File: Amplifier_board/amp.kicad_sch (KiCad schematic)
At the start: 42 parts, among them J11 Conn_01x03_Pin, J15 Conn_01x03_Pin, U4 TPA3111D1PWPR

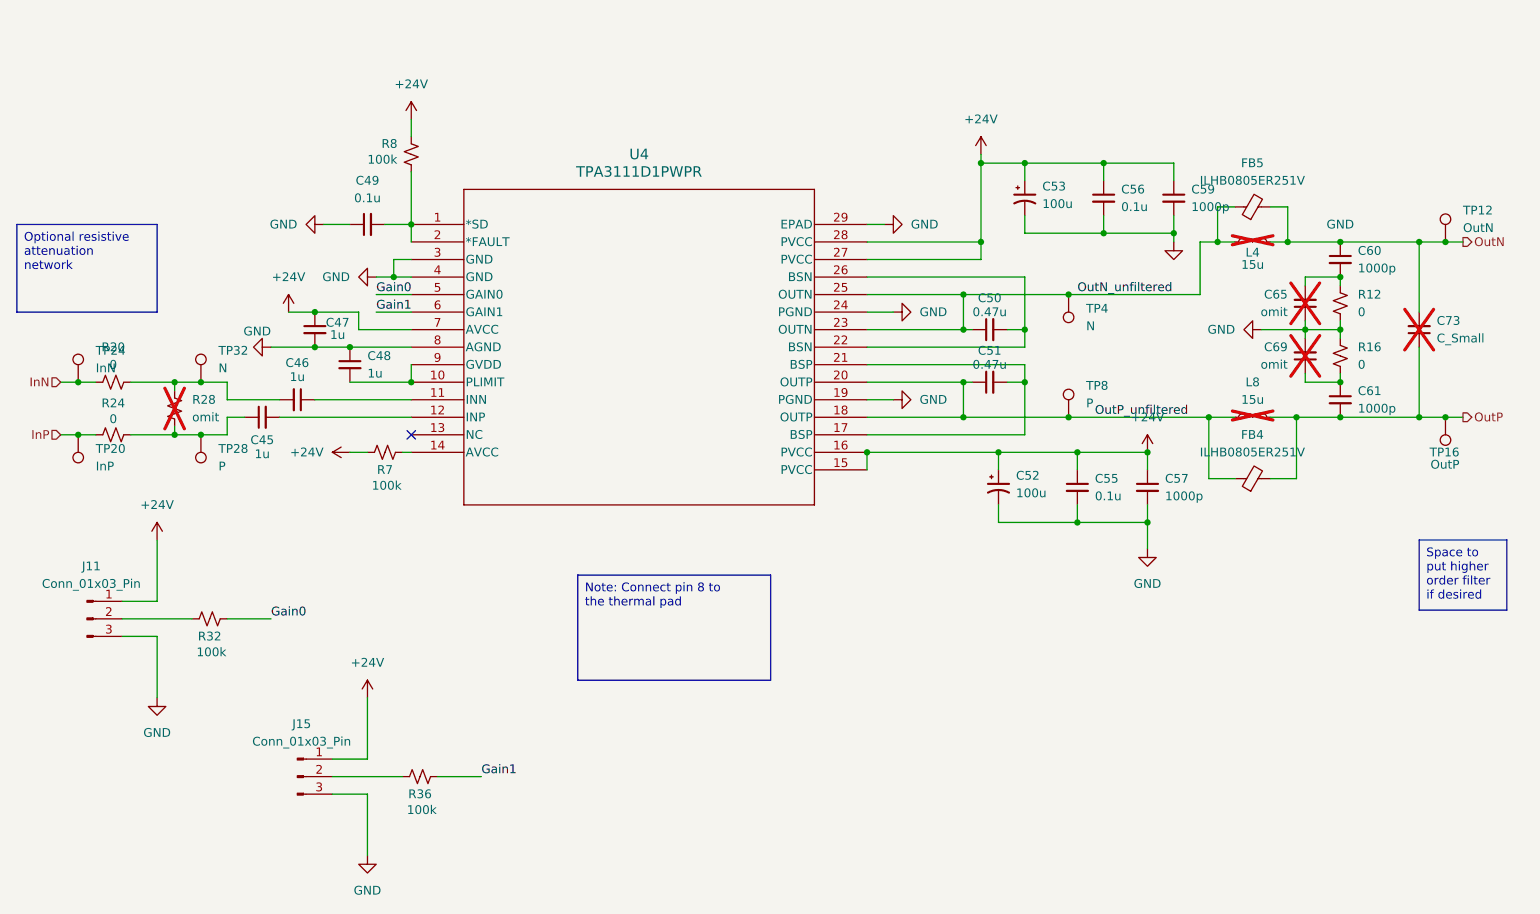
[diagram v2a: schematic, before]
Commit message: Separated AVDD and PVDD on amplifier board
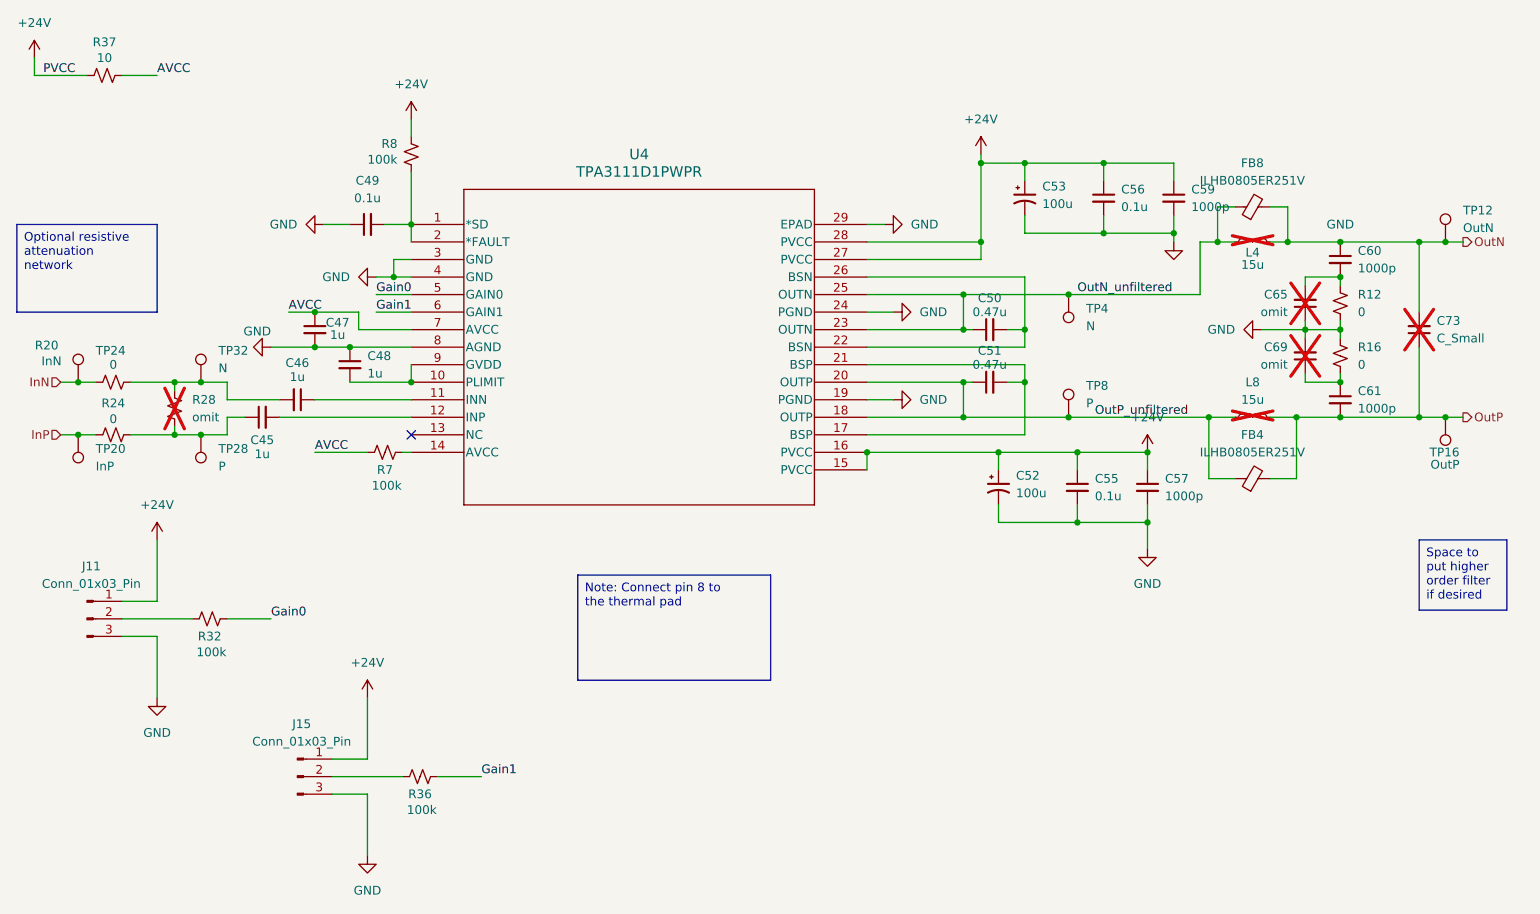
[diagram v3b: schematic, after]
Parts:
- added R37: 10, Capacitor_SMD:C_0805_2012Metric_Pad1.18x1.45mm_HandSolder, symbol Device:R_Small_US
- renumbered FB5 to FB8
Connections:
- net +24V: now also R37.1; no longer C47.1, R7.1, U4.7 (AVCC)
- new net AVCC: C47.1, R37.2, R7.1, U4.7 (AVCC)
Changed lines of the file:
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@@
 	(wire
 		(pts
-			(xy 213.36 62.23) (xy 213.36 64.77)
+			(xy 60.96 41.91) (xy 66.04 41.91)
 		)
 		(stroke
@@
 	(wire
 		(pts
-			(xy 72.39 93.98) (xy 76.2 93.98)
+			(xy 213.36 62.23) (xy 213.36 64.77)
 		)
 		(stroke
@@
 	(wire
 		(pts
-			(xy 93.98 96.52) (xy 96.52 96.52)
+			(xy 72.39 93.98) (xy 76.2 93.98)
 		)
 		(stroke
@@
 	(wire
 		(pts
+			(xy 48.26 39.37) (xy 48.26 41.91)
+		)
+		(stroke
+			(width 0)
+			(type default)
+		)
+	)
+	(wire
+		(pts
 			(xy 102.87 91.44) (xy 83.82 91.44)
 		)
@@
 	(wire
 		(pts
+			(xy 88.9 96.52) (xy 96.52 96.52)
+		)
+		(stroke
+			(width 0)
+			(type default)
+		)
+	)
+	(wire
+		(pts
 			(xy 209.55 106.68) (xy 209.55 104.14)
 		)
@@
 	(wire
 		(pts
+			(xy 48.26 41.91) (xy 55.88 41.91)
+		)
+		(stroke
+			(width 0)
+			(type default)
+		)
+	)
+	(wire
+		(pts
 			(xy 182.88 86.36) (xy 184.15 86.36)
 		)
@@
 		)
 	)
+	(label "AVCC"
+		(at 88.9 96.52 0)
+		(fields_autoplaced yes)
+		(effects
+			(font
+				(size 1.27 1.27)
+			)
+			(justify left bottom)
+		)
+	)
 	(label "OutN_unfiltered"
 		(at 199.39 73.66 0)
@@
 		)
 	)
+	(label "PVCC"
+		(at 49.53 41.91 0)
+		(fields_autoplaced yes)
+		(effects
+			(font
+				(size 1.27 1.27)
+			)
+			(justify left bottom)
+		)
+	)
+	(label "AVCC"
+		(at 66.04 41.91 0)
+		(fields_autoplaced yes)
+		(effects
+			(font
+				(size 1.27 1.27)
+			)
+			(justify left bottom)
+		)
+	)
 	(label "Gain0"
 		(at 97.79 73.66 0)
@@
 		)
 	)
+	(label "AVCC"
+		(at 85.09 76.2 0)
+		(fields_autoplaced yes)
+		(effects
+			(font
+				(size 1.27 1.27)
+			)
+			(justify left bottom)
+		)
+	)
 	(label "Gain1"
 		(at 113.03 143.51 0)
@@
 	)
 	(symbol
+		(lib_id "power:+24V")
+		(at 48.26 39.37 0)
+		(unit 1)
+		(exclude_from_sim no)
+		(in_bom yes)
+		(on_board yes)
+		(dnp no)
+		(fields_autoplaced yes)
+		(property "Reference" "#PWR04"
+			(at 48.26 43.18 0)
+			(effects
+				(font
+					(size 1.27 1.27)
+				)
+				(hide yes)
+			)
+		)
+		(property "Value" "+24V"
+			(at 48.26 34.29 0)
+			(effects
+				(font
+					(size 1.27 1.27)
+				)
+			)
+		)
+		(property "Footprint" ""
+			(at 48.26 39.37 0)
+			(effects
+				(font
+					(size 1.27 1.27)
+				)
+				(hide yes)
+			)
+		)
+		(property "Datasheet" ""
+			(at 48.26 39.37 0)
+			(effects
+				(font
+					(size 1.27 1.27)
+				)
+				(hide yes)
+			)
+		)
+		(property "Description" "Power symbol creates a global label with name \"+24V\""
+			(at 48.26 39.37 0)
+			(effects
+				(font
+					(size 1.27 1.27)
+				)
+				(hide yes)
+			)
+		)
+		(pin "1"
+		)
+		(instances
+			(project "Amplifier_board"
+				(path "/991395a4-3885-4774-b551-0bfe029123d3/1a21d9eb-2329-48b7-8877-ba841ad5b065"
+					(reference "#PWR027")
+					(unit 1)
+				)
+				(path "/991395a4-3885-4774-b551-0bfe029123d3/26541e86-2f42-461f-bb67-92277cc28a80"
+					(reference "#PWR04")
+					(unit 1)
+				)
+				(path "/991395a4-3885-4774-b551-0bfe029123d3/e8898fe0-55dc-4973-83e9-f265cc01a132"
+					(reference "#PWR023")
+					(unit 1)
+				)
+				(path "/991395a4-3885-4774-b551-0bfe029123d3/eadc8ba5-6d36-4b46-a20f-2896249de991"
+					(reference "#PWR08")
+					(unit 1)
+				)
+			)
+		)
+	)
+	(symbol
 		(lib_id "Device:C_Small")
 		(at 232.41 82.55 0)
@@
 	)
 	(symbol
+		(lib_id "Device:R_Small_US")
+		(at 58.42 41.91 90)
+		(unit 1)
+		(exclude_from_sim no)
+		(in_bom yes)
+		(on_board yes)
+		(dnp no)
+		(property "Reference" "R37"
+			(at 58.42 37.084 90)
+			(effects
+				(font
+					(size 1.27 1.27)
+				)
+			)
+		)
+		(property "Value" "10"
+			(at 58.42 39.37 90)
+			(effects
+				(font
+					(size 1.27 1.27)
+				)
+			)
+		)
+		(property "Footprint" "Capacitor_SMD:C_0805_2012Metric_Pad1.18x1.45mm_HandSolder"
+			(at 58.42 41.91 0)
+			(effects
+				(font
+					(size 1.27 1.27)
+				)
+				(hide yes)
+			)
+		)
+		(property "Datasheet" "~"
+			(at 58.42 41.91 0)
+			(effects
+				(font
+					(size 1.27 1.27)
+				)
+				(hide yes)
+			)
+		)
+		(property "Description" "Resistor, small US symbol"
+			(at 58.42 41.91 0)
+			(effects
+				(font
+					(size 1.27 1.27)
+				)
+				(hide yes)
+			)
+		)
+		(pin "1"
+		)
+		(pin "2"
+		)
+		(instances
+			(project ""
+				(path "/991395a4-3885-4774-b551-0bfe029123d3/1a21d9eb-2329-48b7-8877-ba841ad5b065"
+					(reference "R40")
+					(unit 1)
+				)
+				(path "/991395a4-3885-4774-b551-0bfe029123d3/26541e86-2f42-461f-bb67-92277cc28a80"
+					(reference "R37")
+					(unit 1)
+				)
+				(path "/991395a4-3885-4774-b551-0bfe029123d3/e8898fe0-55dc-4973-83e9-f265cc01a132"
+					(reference "R39")
+					(unit 1)
+				)
+				(path "/991395a4-3885-4774-b551-0bfe029123d3/eadc8ba5-6d36-4b46-a20f-2896249de991"
+					(reference "R38")
+					(unit 1)
+				)
+			)
+		)
+	)
+	(symbol
 		(lib_id "Device:C_Small")
 		(at 213.36 59.69 0)
@@
 		(dnp no)
 		(fields_autoplaced yes)
-		(property "Reference" "FB5"
+		(property "Reference" "FB8"
 			(at 224.7519 54.61 90)
 			(effects
@@
 		(dnp no)
 		(property "Reference" "R20"
-			(at 59.69 81.28 90)
+			(at 50.038 81.026 90)
 			(effects
 				(font
@@
 	(symbol
 		(lib_id "power:+24V")
-		(at 93.98 96.52 90)
-		(unit 1)
-		(exclude_from_sim no)
-		(in_bom yes)
-		(on_board yes)
-		(dnp no)
-		(fields_autoplaced yes)
-		(property "Reference" "#PWR063"
-			(at 97.79 96.52 0)
-			(effects
-				(font
-					(size 1.27 1.27)
-				)
-				(hide yes)
-			)
-		)
-		(property "Value" "+24V"
-			(at 90.17 96.5199 90)
-			(effects
-				(font
-					(size 1.27 1.27)
-				)
-				(justify left)
-			)
-		)
-		(property "Footprint" ""
-			(at 93.98 96.52 0)
-			(effects
-				(font
-					(size 1.27 1.27)
-				)
-				(hide yes)
-			)
-		)
-		(property "Datasheet" ""
-			(at 93.98 96.52 0)
-			(effects
-				(font
-					(size 1.27 1.27)
-				)
-				(hide yes)
-			)
-		)
-		(property "Description" "Power symbol creates a global label with name \"+24V\""
-			(at 93.98 96.52 0)
-			(effects
-				(font
-					(size 1.27 1.27)
-				)
-				(hide yes)
-			)
-		)
-		(pin "1"
-		)
-		(instances
-			(project "Amplifier_board"
-				(path "/991395a4-3885-4774-b551-0bfe029123d3/1a21d9eb-2329-48b7-8877-ba841ad5b065"
-					(reference "#PWR063")
-					(unit 1)
-				)
-				(path "/991395a4-3885-4774-b551-0bfe029123d3/26541e86-2f42-461f-bb67-92277cc28a80"
-					(reference "#PWR08")
-					(unit 1)
-				)
-				(path "/991395a4-3885-4774-b551-0bfe029123d3/e8898fe0-55dc-4973-83e9-f265cc01a132"
-					(reference "#PWR045")
-					(unit 1)
-				)
-				(path "/991395a4-3885-4774-b551-0bfe029123d3/eadc8ba5-6d36-4b46-a20f-2896249de991"
-					(reference "#PWR027")
-					(unit 1)
-				)
-			)
-		)
-	)
-	(symbol
-		(lib_id "power:+24V")
 		(at 66.04 109.22 0)
 		(unit 1)
@@
 		(on_board yes)
 		(dnp no)
-		(fields_autoplaced yes)
 		(property "Reference" "TP24"
 			(at 57.15 81.7879 0)
@@
 		)
 		(property "Value" "InN"
-			(at 57.15 84.3279 0)
+			(at 49.276 83.312 0)
 			(effects
 				(font
@@
 					(unit 1)
 				)
-			)
-		)
-	)
-	(symbol
-		(lib_id "power:+24V")
-		(at 85.09 76.2 0)
-		(unit 1)
-		(exclude_from_sim no)
-		(in_bom yes)
-		(on_board yes)
-		(dnp no)
-		(fields_autoplaced yes)
-		(property "Reference" "#PWR059"
-			(at 85.09 80.01 0)
-			(effects
-				(font
-					(size 1.27 1.27)
-				)
-				(hide yes)
-			)
-		)
-		(property "Value" "+24V"
-			(at 85.09 71.12 0)
-			(effects
-				(font
-					(size 1.27 1.27)
-				)
-			)
-		)
-		(property "Footprint" ""
-			(at 85.09 76.2 0)
-			(effects
-				(font
-					(size 1.27 1.27)
-				)
-				(hide yes)
-			)
-		)
-		(property "Datasheet" ""
-			(at 85.09 76.2 0)
-			(effects
-				(font
-					(size 1.27 1.27)
-				)
-				(hide yes)
-			)
-		)
-		(property "Description" "Power symbol creates a global label with name \"+24V\""
-			(at 85.09 76.2 0)
-			(effects
-				(font
-					(size 1.27 1.27)
-				)
-				(hide yes)
-			)
-		)
-		(pin "1"
-		)
-		(instances
-			(project "Amplifier_board"
-				(path "/991395a4-3885-4774-b551-0bfe029123d3/1a21d9eb-2329-48b7-8877-ba841ad5b065"
-					(reference "#PWR059")
-					(unit 1)
-				)
-				(path "/991395a4-3885-4774-b551-0bfe029123d3/26541e86-2f42-461f-bb67-92277cc28a80"
-					(reference "#PWR04")
-					(unit 1)
-				)
-				(path "/991395a4-3885-4774-b551-0bfe029123d3/e8898fe0-55dc-4973-83e9-f265cc01a132"
-					(reference "#PWR041")
-					(unit 1)
-				)
-				(path "/991395a4-3885-4774-b551-0bfe029123d3/eadc8ba5-6d36-4b46-a20f-2896249de991"
-					(reference "#PWR023")
-					(unit 1)
-				)

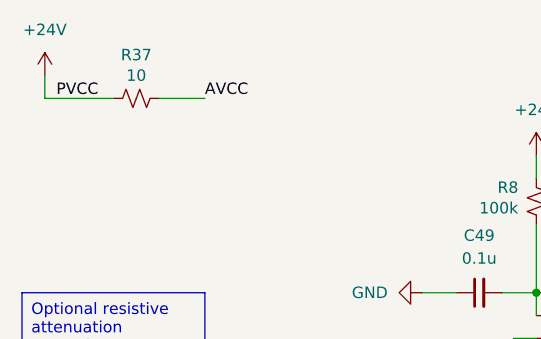
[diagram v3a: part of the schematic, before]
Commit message: Updated ribbon connector on amp board
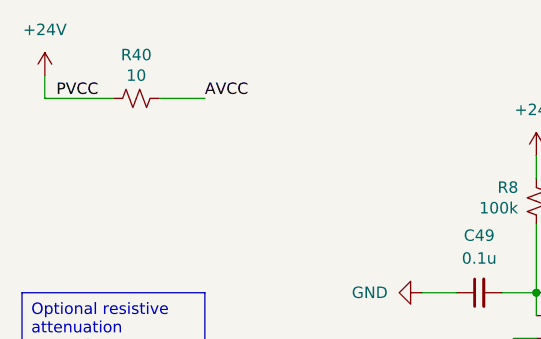
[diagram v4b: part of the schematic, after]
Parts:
- renumbered R37 to R40
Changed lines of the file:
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@@
 		(dnp no)
 		(fields_autoplaced yes)
-		(property "Reference" "#PWR04"
+		(property "Reference" "#PWR027"
 			(at 48.26 43.18 0)
 			(effects
@@
 		(on_board yes)
 		(dnp no)
-		(property "Reference" "R37"
+		(property "Reference" "R40"
 			(at 58.42 37.084 90)
 			(effects

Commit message: generated gerber files
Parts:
- renumbered C45 to C1, C55 to C10, C56 to C11, C57 to C12, C59 to C13, C46 to C2, C47 to C3, C48 to C4, C49 to C5, C60 to C54, C61 to C58, C50 to C6, C65 to C62, C69 to C66, C51 to C7, C73 to C70, C52 to C8, C53 to C9, FB4 to FB1, FB8 to FB5, J15 to J12, J11 to J8, L4 to L1, L8 to L5, R7 to R1, R16 to R13, R20 to R17, R8 to R2, R24 to R21, R28 to R25, R32 to R29, R36 to R33, R40 to R37, R12 to R9, TP4 to TP1, TP16 to TP13, TP20 to TP17, TP24 to TP21, TP28 to TP25, TP32 to TP29, TP8 to TP5, TP12 to TP9, U4 to U1
